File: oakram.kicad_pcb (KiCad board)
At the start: 2 copper layers, 42.5 x 54 mm, 20 parts, among them U1 IS41C16105C, U2 IS41C16105C, X1 ZIP40, X2 ZIP40

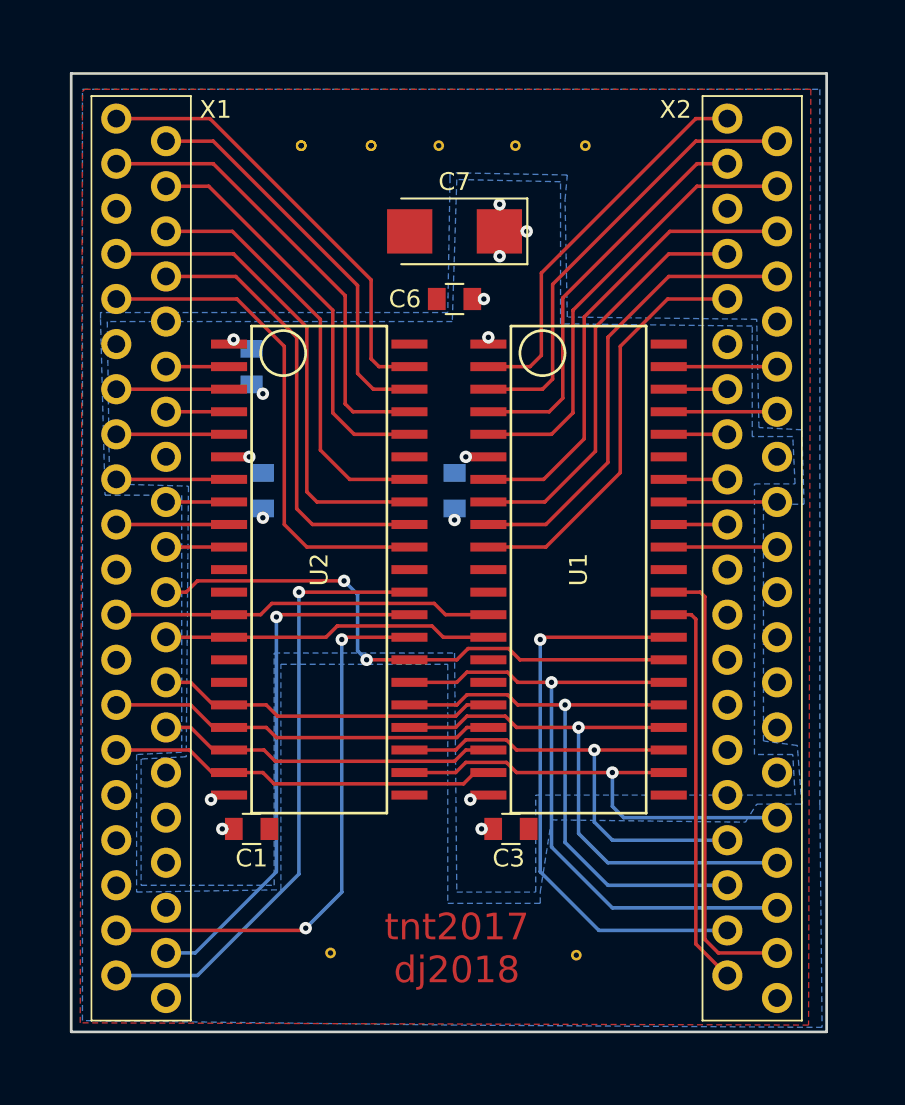
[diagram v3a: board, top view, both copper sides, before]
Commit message: oakramv2.zip from https://stardot.org.uk/forums/viewtopic.php?f=16&t=11214&start=270#p193151 -- danielj ordered a set of these from JLC and they worked
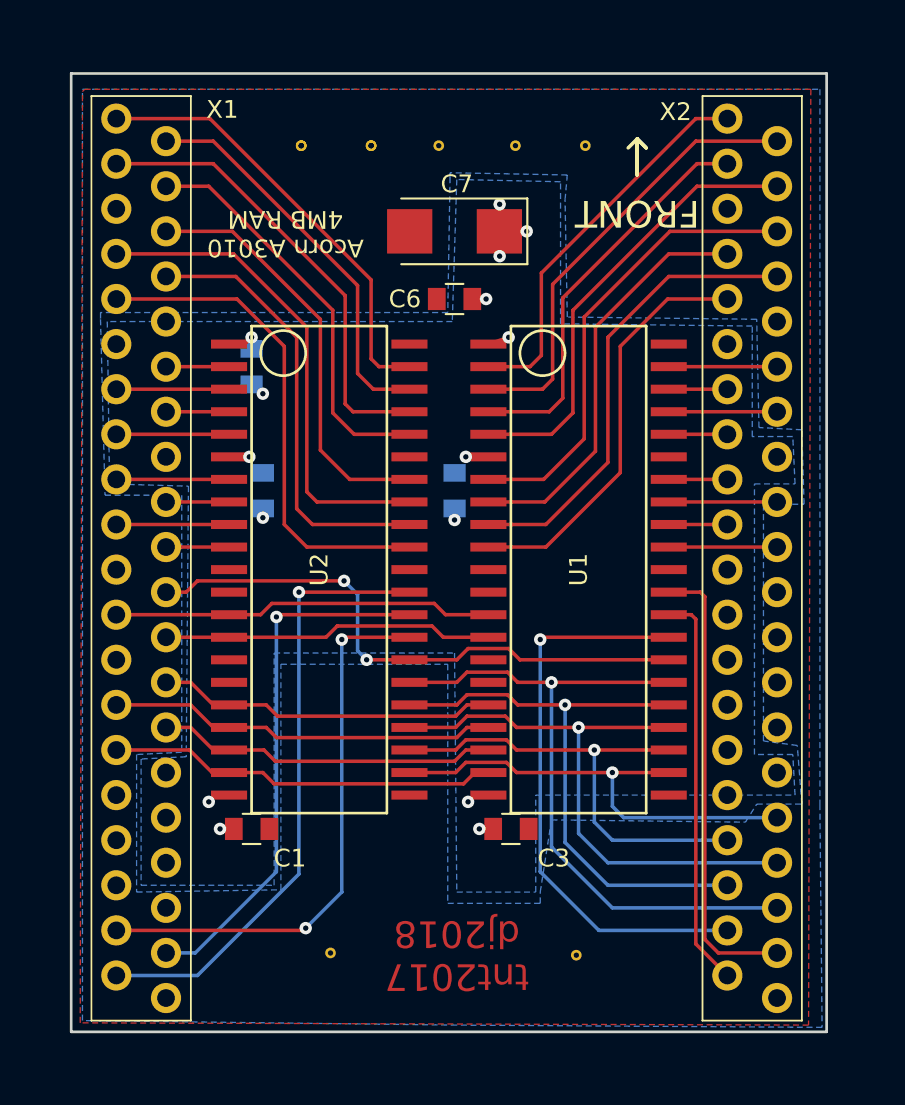
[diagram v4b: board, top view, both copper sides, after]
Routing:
- net VCC: track 12.6 -> 15.5 mm
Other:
- board text added: "Acorn A3010 4MB RAM"
- board text added: "FRONT"
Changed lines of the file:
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@@
-(kicad_pcb (version 20171130) (host pcbnew no-vcs-found-3ad3869~61~ubuntu17.10.1)
+(kicad_pcb (version 4) (host pcbnew 4.0.7)
   (general
+    (links 108)
+    (no_connects 1)
+    (area 119.304999 73.584999 178.665 136.050001)
     (thickness 1.6)
-    (drawings 9)
-    (tracks 276)
+    (drawings 16)
+    (tracks 277)
     (zones 0)
     (modules 20)
@@
     (31 B.Cu signal)
     (32 B.Adhes user)
-    (33 F.Adhes user)
+    (33 F.Adhes user hide)
     (34 B.Paste user)
     (35 F.Paste user)
     (36 B.SilkS user)
     (37 F.SilkS user)
-    (38 B.Mask user)
+    (38 B.Mask user hide)
     (39 F.Mask user)
     (40 Dwgs.User user)
@@
     (visible_elements 7FFFFFFF)
     (pcbplotparams
-      (layerselection 0x00030_ffffffff)
+      (layerselection 0x010f0_80000001)
       (usegerberextensions false)
       (usegerberattributes true)
-      (usegerberadvancedattributes false)
-      (creategerberjobfile false)
       (excludeedgelayer true)
       (linewidth 0.100000)
@@
       (hpglpenspeed 20)
       (hpglpendiameter 15)
+      (hpglpenoverlay 2)
       (psnegative false)
       (psa4output false)
@@
       (outputformat 1)
       (mirror false)
-      (drillshape 1)
+      (drillshape 0)
       (scaleselection 1)
-      (outputdirectory ""))
+      (outputdirectory gerbers))
   )
   (net 0 "")
@@
   (module oakram:ZIP40-P-475-1.27 (layer F.Cu)
     (at 123.32 100.33)
-    (fp_text reference X1 (at 4.188 -24.638) (layer F.SilkS)
+    (fp_text reference X1 (at 4.569 -24.638) (layer F.SilkS)
       (effects (font (size 1 1) (thickness 0.15)))
     )
@@
   (module oakram:ZIP40-P-475-1.27 (layer F.Cu)
     (at 157.734 100.33)
-    (fp_text reference X2 (at -4.318 -24.638) (layer F.SilkS)
+    (fp_text reference X2 (at -4.318 -24.511) (layer F.SilkS)
       (effects (font (size 1 1) (thickness 0.15)))
     )
@@
     (tags "capacitor 0805")
     (attr smd)
-    (fp_text reference C1 (at 0 1.651) (layer F.SilkS)
+    (fp_text reference C1 (at 2.159 1.651) (layer F.SilkS)
       (effects (font (size 1 1) (thickness 0.15)))
     )
@@
     (tags "capacitor 0805")
     (attr smd)
-    (fp_text reference C3 (at -0.127 1.651) (layer F.SilkS)
+    (fp_text reference C3 (at 2.413 1.651) (layer F.SilkS)
       (effects (font (size 1 1) (thickness 0.15)))
     )
@@
     (tags "capacitor tantalum smd")
     (attr smd)
-    (fp_text reference C7 (at 0 2.794 180) (layer F.SilkS)
+    (fp_text reference C7 (at -0.127 2.667 360) (layer F.SilkS)
       (effects (font (size 1 1) (thickness 0.15)))
     )
@@
     )
   )
-  (gr_text "tnt2017\ndj2018" (at 141.097 122.936) (layer F.Cu)
+  (gr_text FRONT (at 151.257 81.534 180) (layer F.SilkS)
+    (effects (font (size 1.5 1.5) (thickness 0.3)))
+  )
+  (gr_line (start 151.257 77.343) (end 150.749 77.851) (angle 90) (layer F.SilkS) (width 0.2))
+  (gr_line (start 151.765 77.851) (end 151.257 77.343) (angle 90) (layer F.SilkS) (width 0.2))
+  (gr_line (start 151.257 77.343) (end 151.765 77.851) (angle 90) (layer F.SilkS) (width 0.2))
+  (gr_line (start 151.257 79.375) (end 151.257 77.343) (angle 90) (layer F.SilkS) (width 0.2))
+  (gr_line (start 151.257 77.47) (end 151.257 79.375) (angle 90) (layer F.SilkS) (width 0.2))
+  (gr_text "Acorn A3010\n4MB RAM" (at 131.445 82.677 180) (layer F.SilkS)
+    (effects (font (size 1 1) (thickness 0.2)))
+  )
+  (gr_text "tnt2017\ndj2018" (at 141.097 123.317 180) (layer F.Cu)
     (effects (font (size 1.5 1.5) (thickness 0.3)))
   )
@@
   (via (at 130.175 91.694) (size 0.7) (drill 0.3) (layers F.Cu B.Cu) (net 56))
   (segment (start 129.54 91.17) (end 129.54 91.313) (width 0.2) (layer B.Cu) (net 56))
+  (segment (start 128.27 88.9) (end 129.159 88.9) (width 0.2) (layer F.Cu) (net 57))
+  (segment (start 129.159 88.9) (end 129.54 88.519) (width 0.2) (layer F.Cu) (net 57))
+  (via (at 129.54 88.519) (size 0.7) (drill 0.3) (layers F.Cu B.Cu) (net 57))
+  (segment (start 129.54 88.519) (end 129.54 89.17) (width 0.2) (layer B.Cu) (net 57))
   (segment (start 128.27 114.3) (end 127.508 114.3) (width 0.2) (layer F.Cu) (net 57))
-  (segment (start 127.508 114.3) (end 127.254 114.554) (width 0.2) (layer F.Cu) (net 57))
-  (via (at 127.254 114.554) (size 0.7) (drill 0.3) (layers F.Cu B.Cu) (net 57))
+  (segment (start 127.508 114.3) (end 127.127 114.681) (width 0.2) (layer F.Cu) (net 57))
+  (via (at 127.127 114.681) (size 0.7) (drill 0.3) (layers F.Cu B.Cu) (net 57))
   (segment (start 142.875 114.3) (end 142.113 114.3) (width 0.2) (layer F.Cu) (net 57))
-  (segment (start 142.113 114.3) (end 141.859 114.554) (width 0.2) (layer F.Cu) (net 57))
-  (via (at 141.859 114.554) (size 0.7) (drill 0.3) (layers F.Cu B.Cu) (net 57))
-  (segment (start 143.145 116.205) (end 142.494 116.205) (width 0.2) (layer F.Cu) (net 57))
-  (via (at 142.494 116.205) (size 0.7) (drill 0.3) (layers F.Cu B.Cu) (net 57))
-  (segment (start 128.54 116.205) (end 127.889 116.205) (width 0.2) (layer F.Cu) (net 57))
-  (via (at 127.889 116.205) (size 0.7) (drill 0.3) (layers F.Cu B.Cu) (net 57))
-  (segment (start 128.27 88.9) (end 128.524 88.646) (width 0.2) (layer F.Cu) (net 57))
-  (via (at 128.524 88.646) (size 0.7) (drill 0.3) (layers F.Cu B.Cu) (net 57))
-  (segment (start 128.27 88.9) (end 128.651 88.9) (width 0.2) (layer F.Cu) (net 57))
+  (segment (start 142.113 114.3) (end 141.732 114.681) (width 0.2) (layer F.Cu) (net 57))
+  (via (at 141.732 114.681) (size 0.7) (drill 0.3) (layers F.Cu B.Cu) (net 57))
+  (segment (start 143.145 116.205) (end 142.367 116.205) (width 0.2) (layer F.Cu) (net 57))
+  (via (at 142.367 116.205) (size 0.7) (drill 0.3) (layers F.Cu B.Cu) (net 57))
+  (segment (start 128.54 116.205) (end 127.762 116.205) (width 0.2) (layer F.Cu) (net 57))
+  (via (at 127.762 116.205) (size 0.7) (drill 0.3) (layers F.Cu B.Cu) (net 57))
   (segment (start 142.875 95.25) (end 141.605 95.25) (width 0.2) (layer F.Cu) (net 57))
   (via (at 141.605 95.25) (size 0.7) (drill 0.3) (layers F.Cu B.Cu) (net 57))
@@
   (via (at 129.413 95.25) (size 0.7) (drill 0.3) (layers F.Cu B.Cu) (net 57))
   (segment (start 129.54 89.17) (end 129.54 88.773) (width 0.2) (layer B.Cu) (net 57))
-  (segment (start 141.97 86.36) (end 142.621 86.36) (width 0.2) (layer F.Cu) (net 57))
-  (via (at 142.621 86.36) (size 0.7) (drill 0.3) (layers F.Cu B.Cu) (net 57))
-  (segment (start 142.875 88.9) (end 142.875 88.519) (width 0.2) (layer F.Cu) (net 57))
-  (via (at 142.875 88.519) (size 0.7) (drill 0.3) (layers F.Cu B.Cu) (net 57))
+  (segment (start 141.97 86.36) (end 142.748 86.36) (width 0.2) (layer F.Cu) (net 57))
+  (via (at 142.748 86.36) (size 0.7) (drill 0.3) (layers F.Cu B.Cu) (net 57))
+  (segment (start 142.875 88.9) (end 144.018 88.519) (width 0.2) (layer F.Cu) (net 57))
+  (via (at 144.018 88.519) (size 0.7) (drill 0.3) (layers F.Cu B.Cu) (net 57))
   (segment (start 143.495 82.55) (end 143.495 83.932) (width 0.2) (layer F.Cu) (net 57))
   (via (at 143.51 83.947) (size 0.7) (drill 0.3) (layers F.Cu B.Cu) (net 57))
@@
   (via (at 143.51 81.026) (size 0.7) (drill 0.3) (layers F.Cu B.Cu) (net 57))
   (segment (start 143.495 81.041) (end 143.51 81.026) (width 0.2) (layer F.Cu) (net 57))
-  (zone (net 0) (net_name "") (layer F.Mask) (hatch full 0.508)
-    (connect_pads (clearance 0.254))
-    (min_thickness 0.254)
-    (fill yes (arc_segments 16) (thermal_gap 0.508) (thermal_bridge_width 0.508))
-    (polygon
-      (pts
-        (xy 136.144 120.142) (xy 146.05 120.142) (xy 146.05 125.984) (xy 136.144 125.984)
-      )
-    )
-  )
   (zone (net 56) (net_name VSS) (layer F.Cu) (hatch edge 0.508)
     (connect_pads (clearance 0.254))
     (min_thickness 0.127)
-    (fill yes (arc_segments 16) (thermal_gap 0.254) (thermal_bridge_width 0.254))
+    (fill yes (arc_segments 16) (thermal_gap 0.254) (thermal_bridge_width 0.508))
     (polygon
       (pts
@@
     (connect_pads (clearance 0.254))
     (min_thickness 0.127)
-    (fill yes (arc_segments 16) (thermal_gap 0.254) (thermal_bridge_width 0.254))
+    (fill yes (arc_segments 16) (thermal_gap 0.254) (thermal_bridge_width 0.508))
     (polygon
       (pts
@@
     (connect_pads (clearance 0.254))
     (min_thickness 0.127)
-    (fill yes (arc_segments 16) (thermal_gap 0.254) (thermal_bridge_width 0.254))
+    (fill yes (arc_segments 16) (thermal_gap 0.254) (thermal_bridge_width 0.508))
     (polygon
       (pts
@@
     )
     (polygon
-      (pts
-        (xy 160.274 111.506) (xy 158.369 111.252) (xy 158.369 97.917) (xy 160.655 97.917) (xy 160.528 93.726)
+      (pts        (xy 160.274 111.506) (xy 158.369 111.252) (xy 158.369 97.917) (xy 160.655 97.917) (xy 160.528 93.726)
         (xy 158.115 93.599) (xy 157.988 87.503) (xy 147.32 87.376) (xy 147.193 80.772) (xy 147.32 79.375)
         (xy 140.716 79.248) (xy 140.716 79.502) (xy 140.589 87.122) (xy 121.031 87.122) (xy 121.031 87.503)
@@
       )
     )
+  )
+  (zone (net 0) (net_name "") (layer F.Mask) (hatch edge 0.508)
+    (connect_pads (clearance 0.254))
+    (min_thickness 0.127)
+    (fill yes (arc_segments 16) (thermal_gap 0.254) (thermal_bridge_width 0.508))
+    (polygon
+      (pts
+        (xy 136.525 120.396) (xy 145.542 120.396) (xy 145.542 125.73) (xy 136.525 125.73)
+      )
+    )

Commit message: Messing around with grounding etc
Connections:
- U1 pad 29: /~OE -> /~OE2
- U2 pad 29: /~OE -> /~OE1
- X1 pad 37: /~OE -> /~OE1
- X2 pad 37: /~OE -> /~OE2
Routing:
- net VCC: track 15.5 -> 82.3 mm
- net /~OE: track 64.0 -> 0.00 mm, vias 3 -> 0
- net /~OE1: track 0.00 -> 31.7 mm, vias 0 -> 2
- net /~OE2: track 0.00 -> 30.8 mm, vias 0 -> 1
- net /A5: track 27.1 -> 24.3 mm
- net /A4: track 26.5 -> 23.8 mm
- net /A6: track 33.0 -> 30.5 mm
- net /A7: track 33.0 -> 31.0 mm
- net /A8: track 38.5 -> 36.9 mm
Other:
- net class Default: clearance 0 -> 0.1524; trace_width 0.25 -> 0.1524
- rule trace_clearance: 0 -> 0.1524
- rule trace_min: 0.2 -> 0.1524

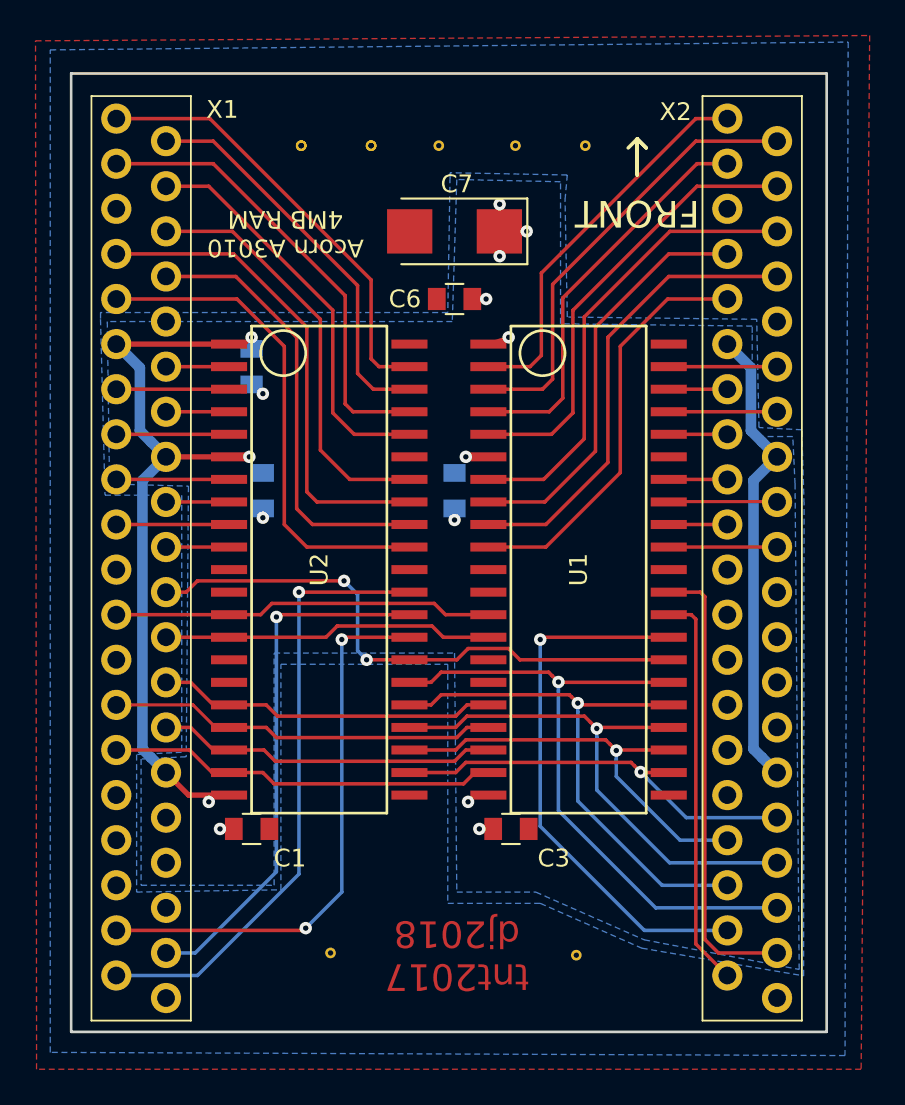
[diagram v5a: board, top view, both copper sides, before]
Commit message: Removed split planes on B.Cu, replaced with one big ground plane and a VCC ring
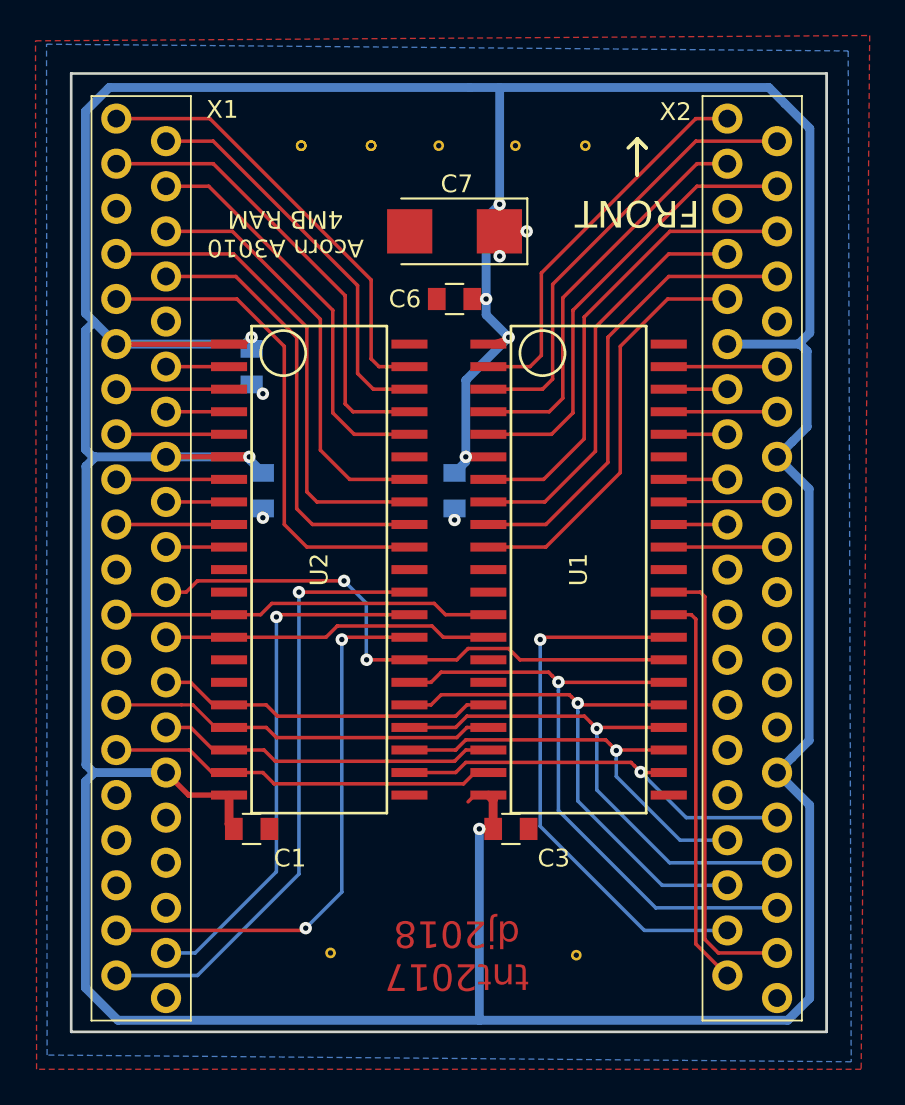
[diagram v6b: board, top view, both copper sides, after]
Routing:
- net VCC: track 82.3 -> 281.0 mm, vias 12 -> 9
- removed copper zone on B.Cu, net VCC

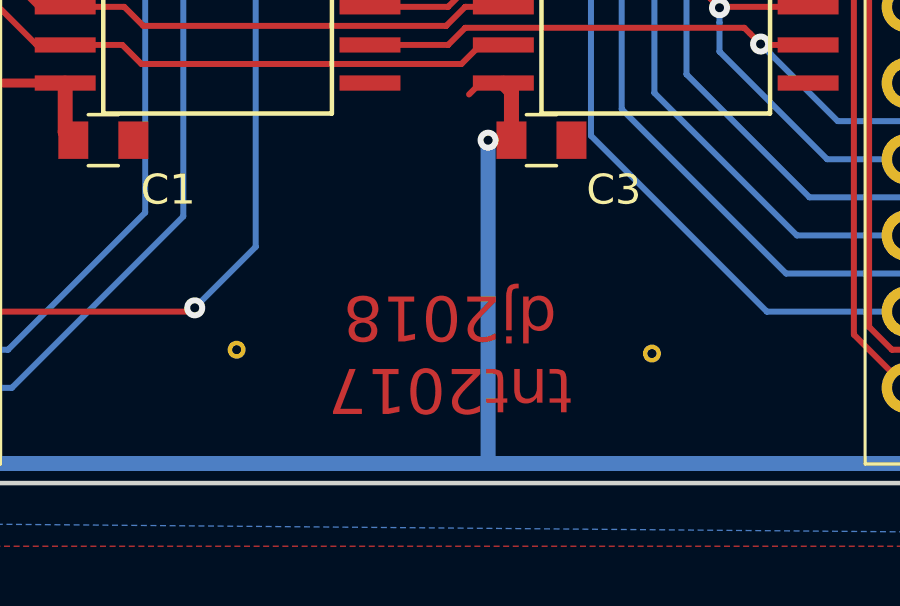
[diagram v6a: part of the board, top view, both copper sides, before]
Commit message: Added pp2019 to author list on F.Cu
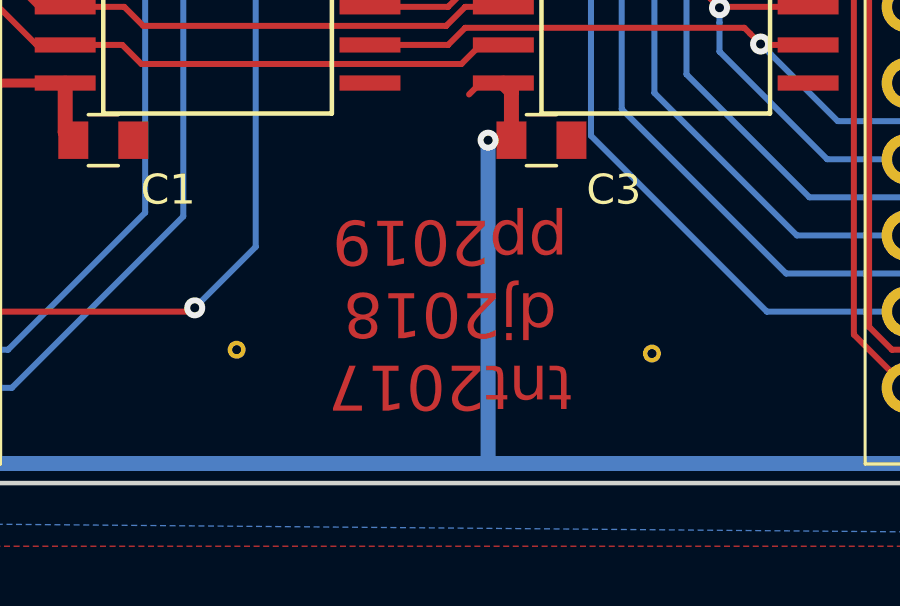
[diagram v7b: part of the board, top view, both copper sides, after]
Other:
- board text added: "tnt2017 dj2018 pp2019"
- board text removed: "tnt2017 dj2018"
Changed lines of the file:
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@@
     (37 F.SilkS user)
     (38 B.Mask user hide)
-    (39 F.Mask user)
+    (39 F.Mask user hide)
     (40 Dwgs.User user)
     (41 Cmts.User user)
@@
   )
   (setup
-    (last_trace_width 0.5)
+    (last_trace_width 0.1524)
     (user_trace_width 0.1778)
     (user_trace_width 0.2)
@@
     (effects (font (size 1 1) (thickness 0.2)))
   )
-  (gr_text "tnt2017\ndj2018" (at 141.097 123.317 180) (layer F.Cu)
+  (gr_text "tnt2017\ndj2018\npp2019" (at 141.097 122 180) (layer F.Cu)
     (effects (font (size 1.5 1.5) (thickness 0.3)))
   )
@@
     (polygon
       (pts
-        (xy 136.525 120.396) (xy 145.542 120.396) (xy 145.542 125.73) (xy 136.525 125.73)
+        (xy 136.42 117.93) (xy 145.77 117.92) (xy 145.76 125.82) (xy 136.42 125.84)
       )
     )
